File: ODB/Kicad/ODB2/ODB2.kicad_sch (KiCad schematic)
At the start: 23 parts, among them U1 STM32F479ZGTx

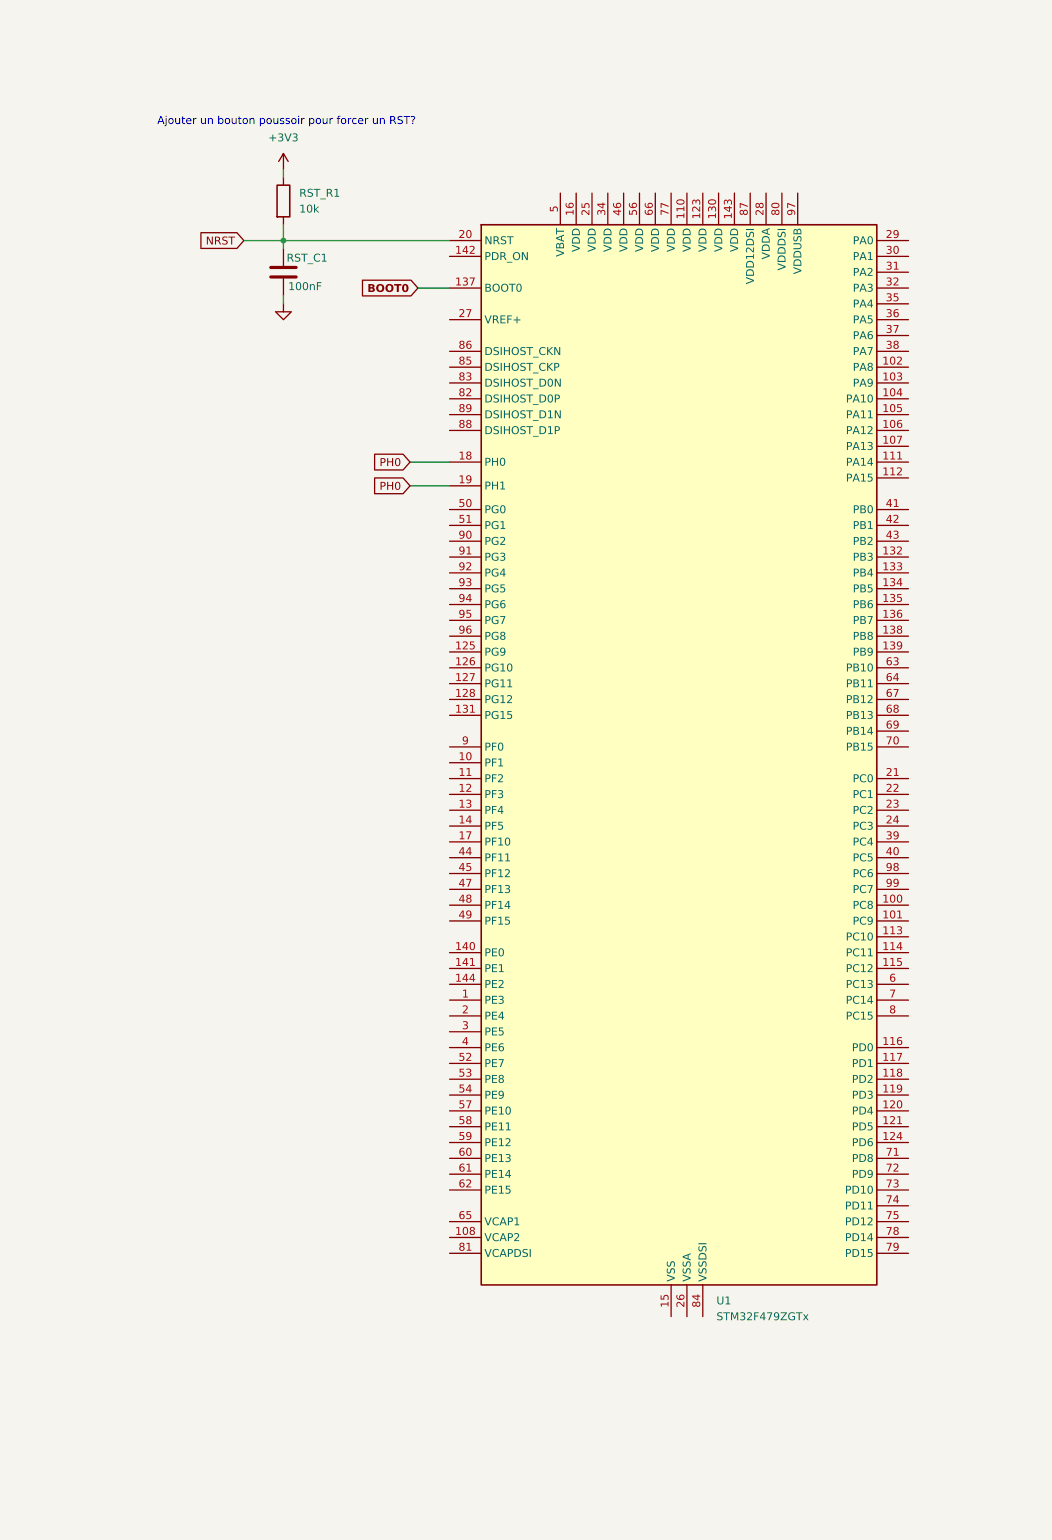
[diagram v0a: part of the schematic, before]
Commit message: fix mcu symbol
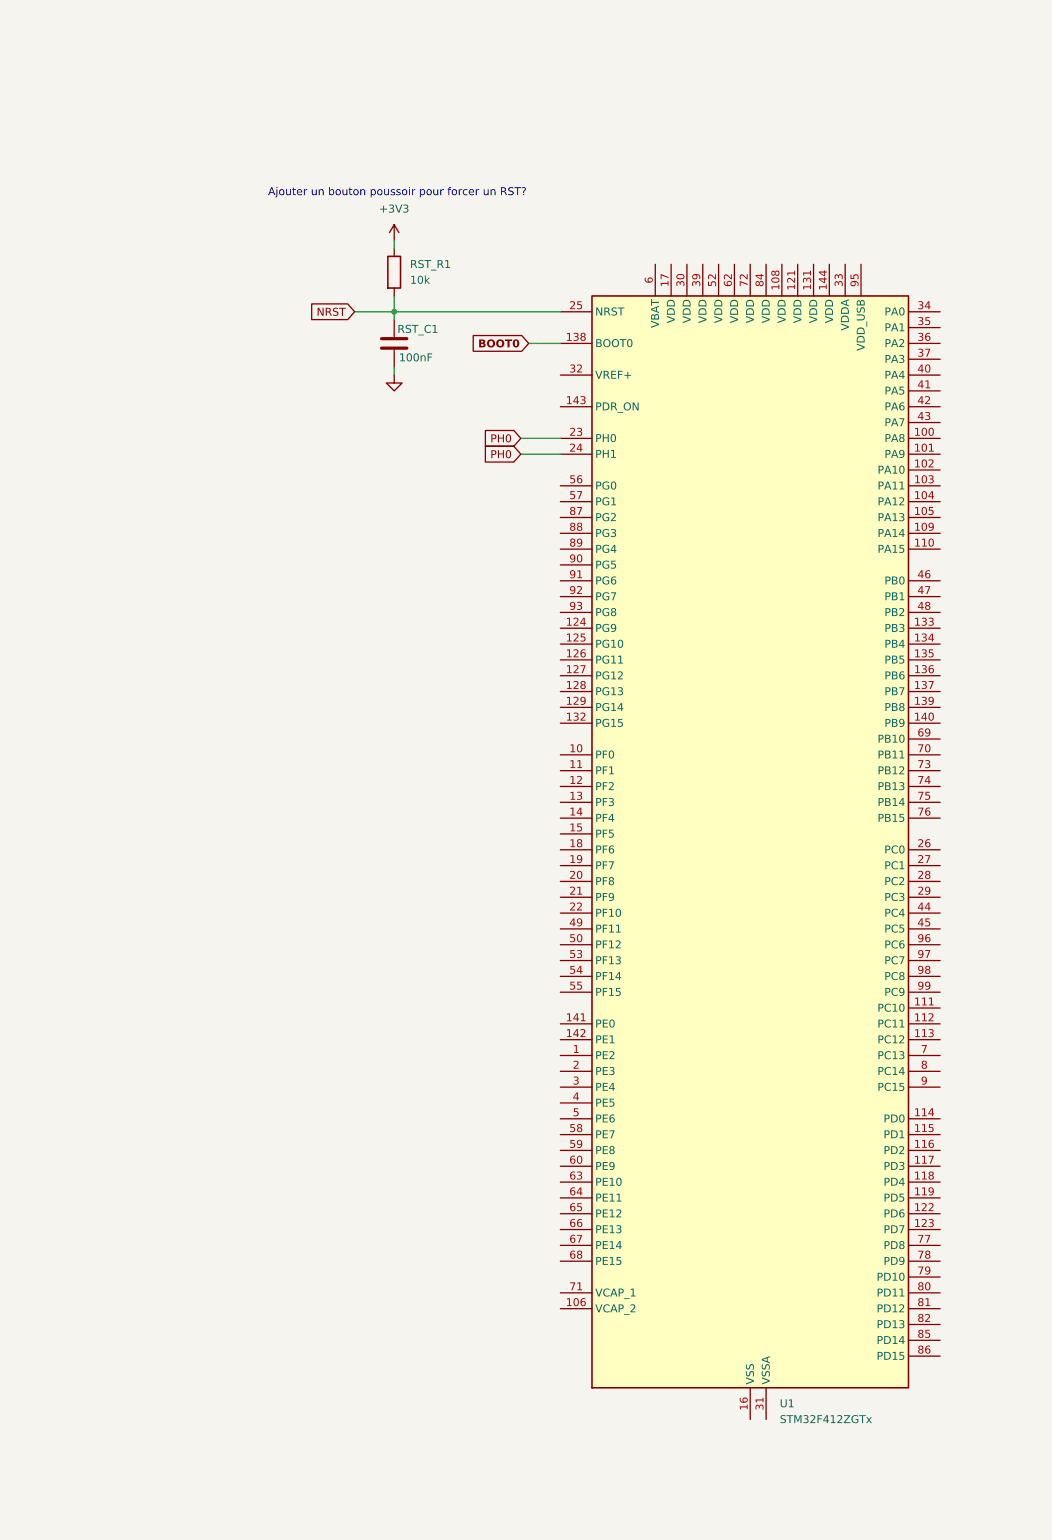
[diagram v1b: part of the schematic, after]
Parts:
- removed U1: STM32F479ZGTx, Package_QFP:LQFP-144_20x20mm_P0.5mm, symbol ODB_Lib:STM32F479ZGTx
- added U1: STM32F412ZGTx, Package_QFP:LQFP-144_20x20mm_P0.5mm, symbol ODB_Lib:STM32F412ZGTx
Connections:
- net BOOT0: now also U1.138 (BOOT0)
- net NRST: now also U1.25 (NRST)
- net PH0: now also U1.23 (PH0), U1.24 (PH1)
- new net: U1.107 (VSS), U1.120 (VSS), U1.130 (VSS), U1.16 (VSS), U1.38 (VSS), U1.51 (VSS), U1.61 (VSS), U1.83 (VSS), U1.94 (VSS)
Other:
- moved on the sheet: RST_C1, RST_R1
